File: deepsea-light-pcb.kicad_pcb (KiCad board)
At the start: 4 copper layers, 124.5 x 56.8 mm, 8 parts, among them CN1 XT60PW-M, U1 Pico, U2 2604-1104, U3 2604-1104, U4 2604-1104, U5 2604-1104, U6 2604-1103, U7 SparkFun_RS485_Breakout

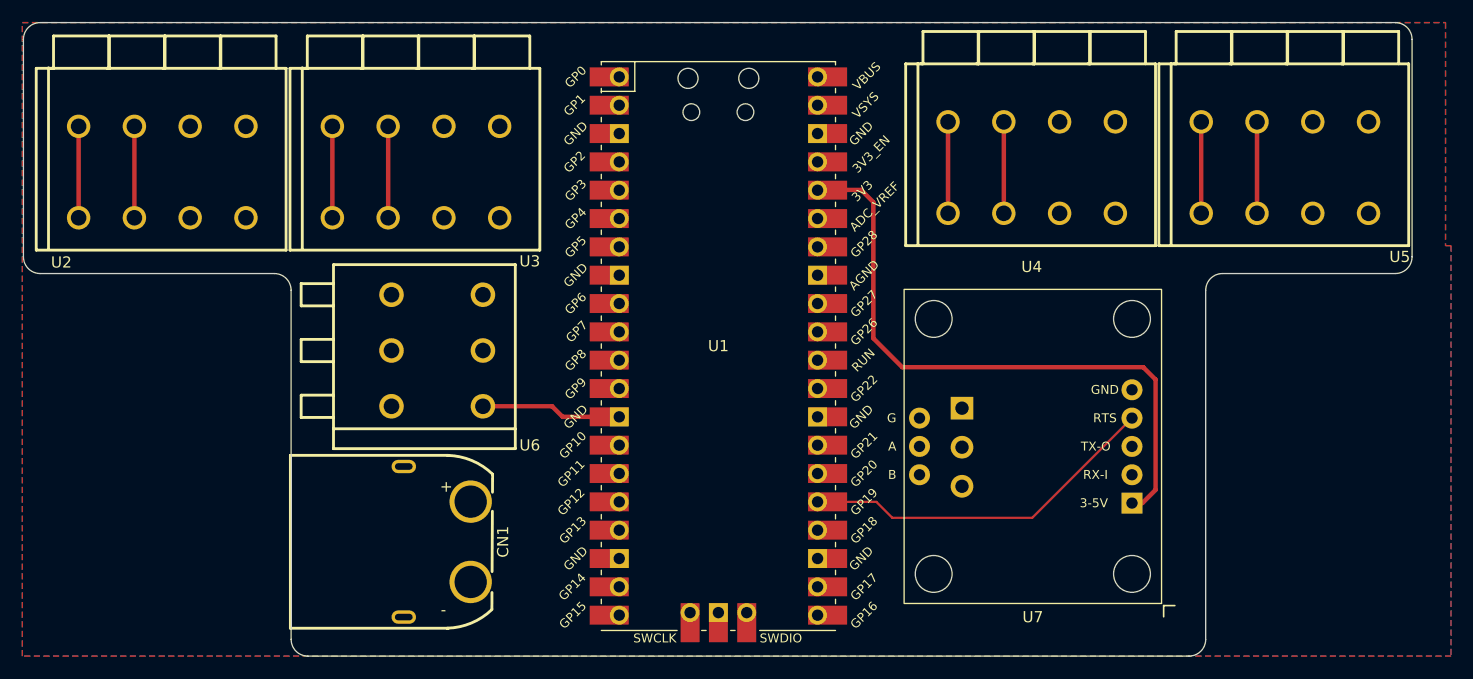
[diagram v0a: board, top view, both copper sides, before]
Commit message: Fix silkscreen
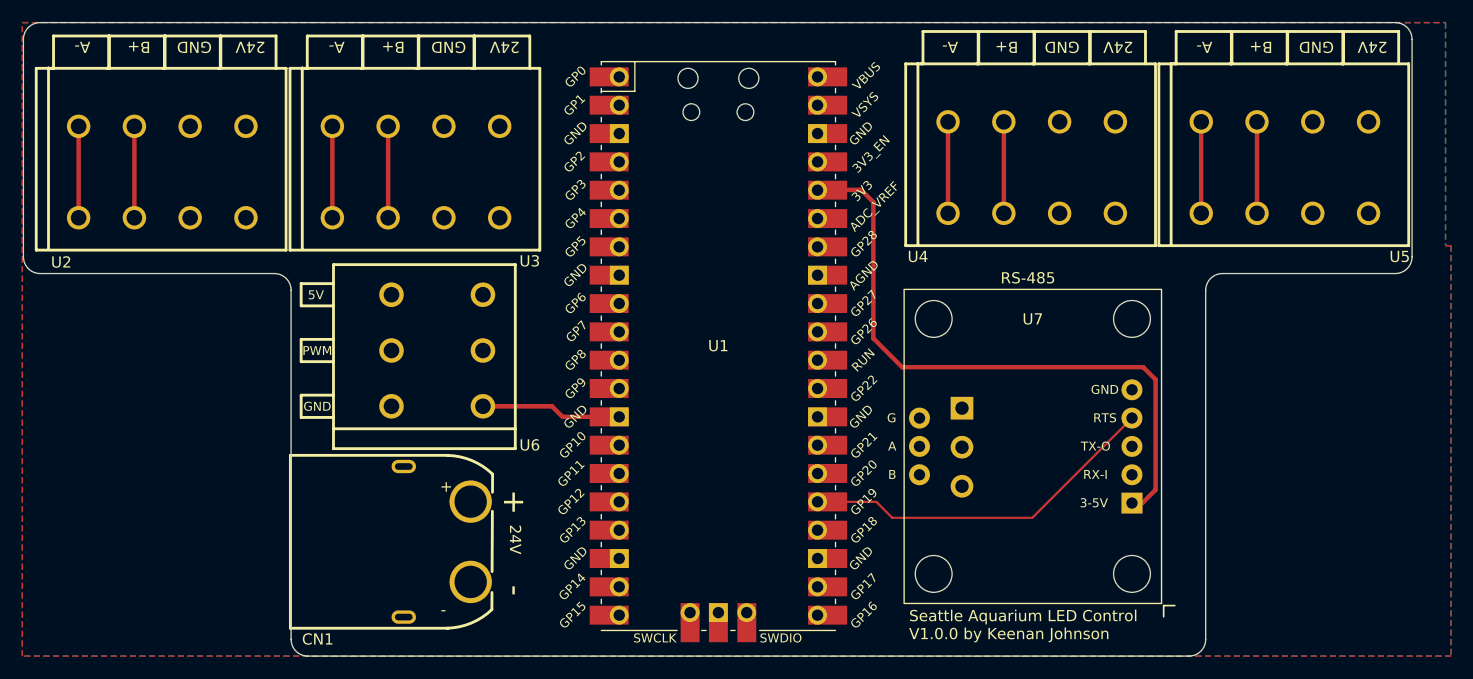
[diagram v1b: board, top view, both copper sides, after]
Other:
- board text added: "+"
- board text added: "-"
- board text added: "24V"
- board text added: "5V"
- board text added: "A-"
- board text added: "B+"
- board text added: "GND"
- board text added: "PWM"
- board text added: "RS-485"
- board text added: "Seattle Aquarium LED Control V1.0.0 by Keenan Johnson"

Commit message: Populate headers for fab only
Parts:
- added J1: PinSocket_1x20_P2.54mm, Deepsea_light_lib:Socket_1x20_P2.54mm_NoPads, F.Cu at (149.5, 83.3)
- added J2: PinSocket_1x20_P2.54mm, Deepsea_light_lib:Socket_1x20_P2.54mm_NoPads, F.Cu at (167.2, 83.3)
- added J3: PinSocket_1x05_P2.54mm, Deepsea_light_lib:Socket_1x05_P2.54mm_NoPads, F.Cu at (195.4, 92.3)
- added J4: PinSocket_1x03_P2.54mm, Deepsea_light_lib:Socket_1x03_P2.54mm_NoPads, F.Cu at (176.4, 92.3)

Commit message: Fix solder connections
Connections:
- U1 pad 41: GND -> unconnected-(U1-SWCLK-Pad41)_1
- U1 pad 43: GND -> unconnected-(U1-SWDIO-Pad43)_1

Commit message: Add stemma
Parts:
- added J5: 250-104, Deepsea_light_lib:CONN-TH_4P-P3.50_250-104, F.Cu at (208.4, 92.7)
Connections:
- U1 pad 19: unconnected-(U1-GPIO14-Pad19) -> /I2C_SDA
- U1 pad 20: unconnected-(U1-GPIO15-Pad20) -> /I2C_SCL
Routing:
- net /I2C_SDA: track 0.00 -> 65.5 mm
- net /I2C_SCL: track 0.00 -> 64.6 mm
- net +3V3: track 57.0 -> 69.8 mm
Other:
- outline, holes or cut-outs redrawn
- board text added: "3V3"
- board text added: "SCL"
- board text added: "SDA"
